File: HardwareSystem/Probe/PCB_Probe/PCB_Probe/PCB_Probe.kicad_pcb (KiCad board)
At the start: 2 copper layers, 37.3 x 162.6 mm, 24 parts, among them J1 Conn_01x15, J2 Conn_01x15, U1 TLC555xP, U2 LP2950CZ-3.0/NOPB

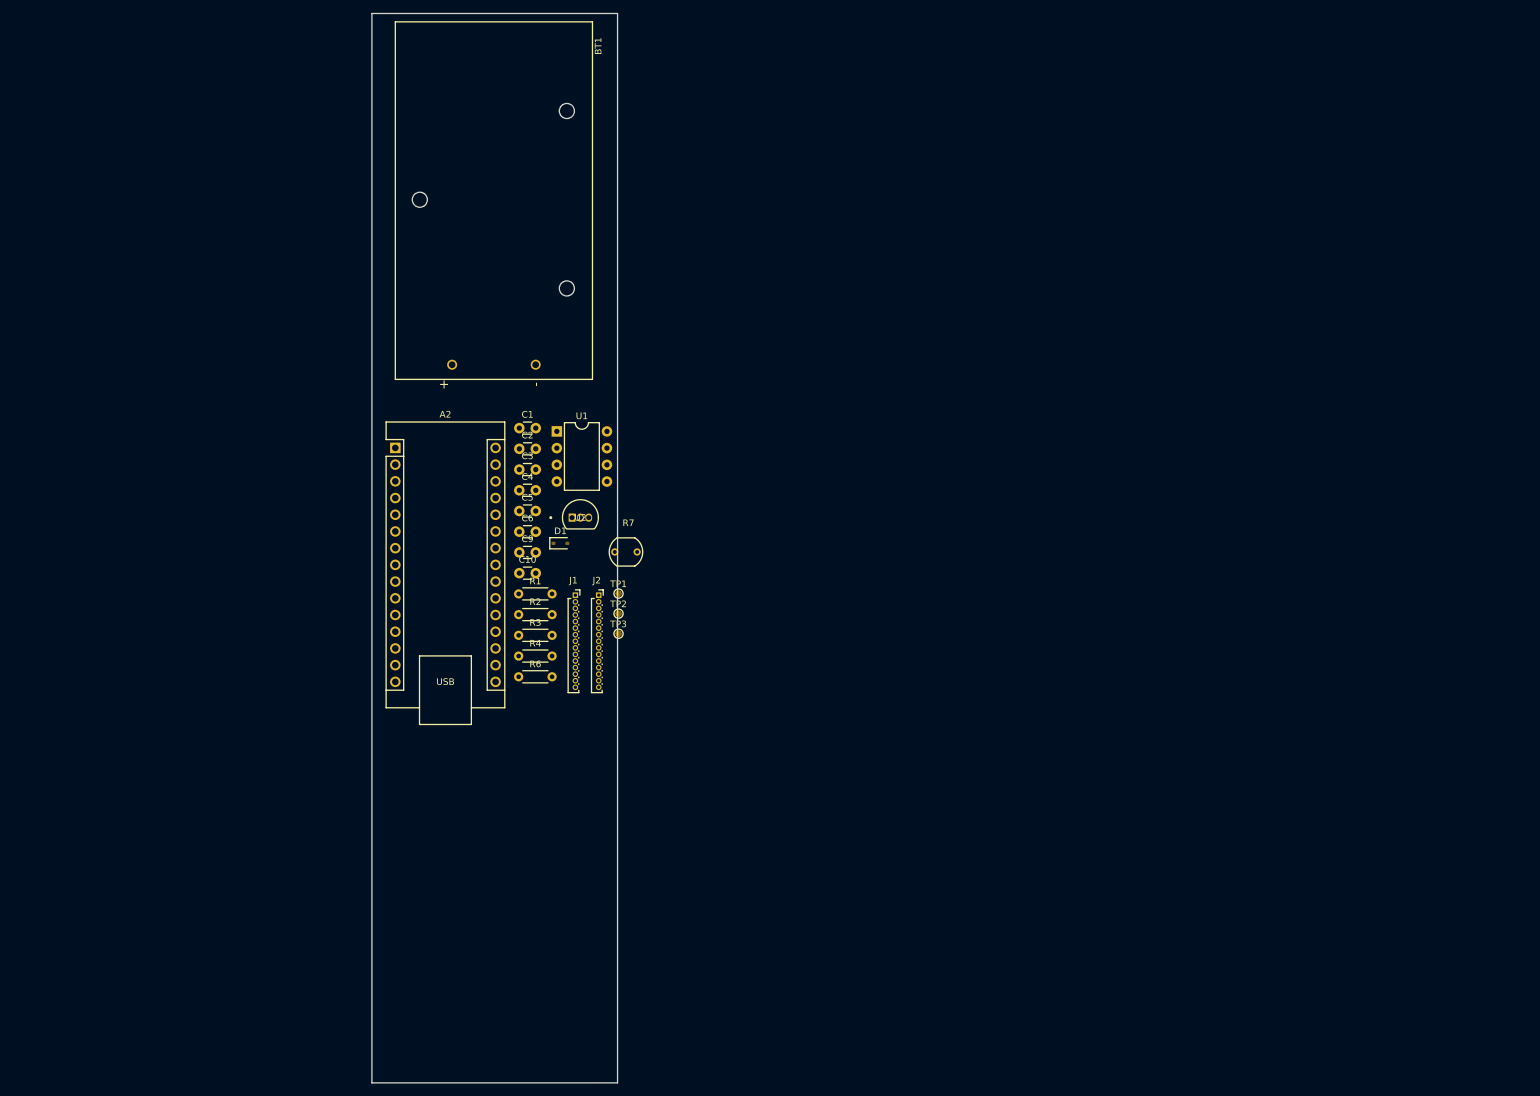
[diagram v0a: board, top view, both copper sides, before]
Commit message: more layout design
Added:
header footprint
pcb margins for probe
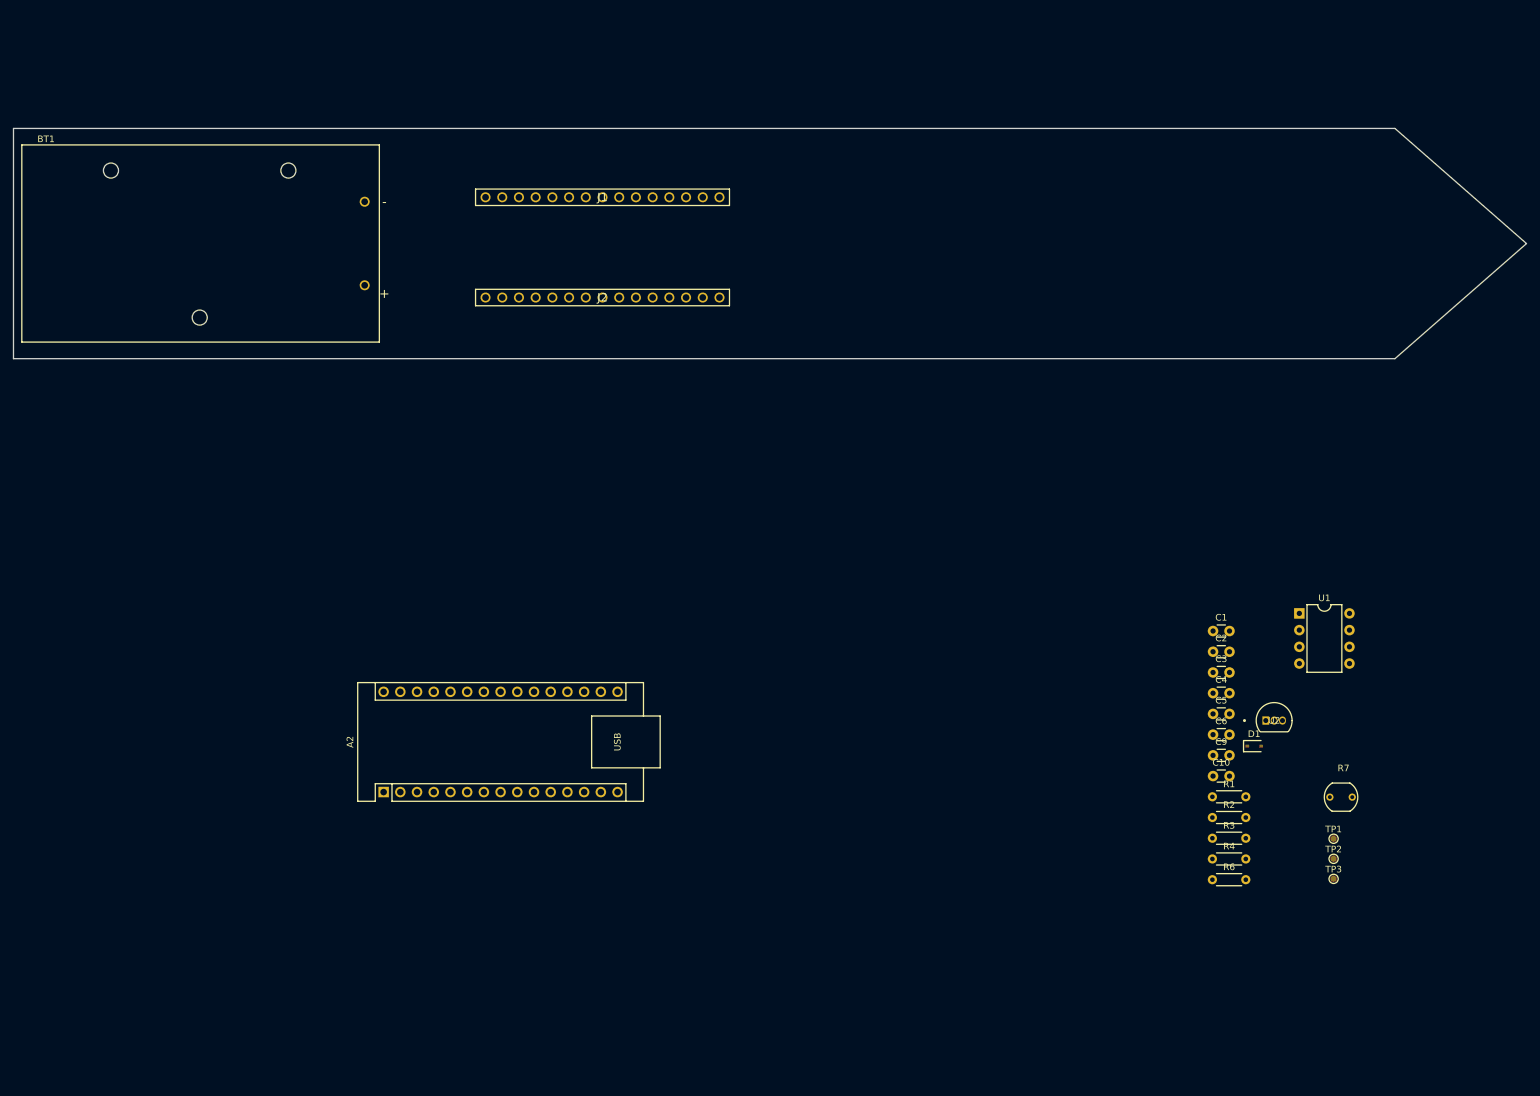
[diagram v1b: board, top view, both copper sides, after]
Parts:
- J1, J2: footprint Connector_PinSocket_1.00mm:PinSocket_1x15_P1.00mm_Vertical -> KiCADv6:PRT16279
- moved U1 116.2 mm to (235.5, 108.7)
- moved R7 114.9 mm to (241.8, 136.7)
- moved TP1 114.9 mm to (240.7, 143.0)
- moved TP2 114.9 mm to (240.7, 146.0)
- moved TP3 114.9 mm to (240.7, 149.1)
- moved D1 109.9 mm to (228.6, 128.9)
- moved R1 109.9 mm to (222.2, 136.6)
- moved R2 109.9 mm to (222.2, 139.8)
- moved R3 109.9 mm to (222.2, 142.9)
- moved R4 109.9 mm to (222.2, 146.1)
- moved R6 109.9 mm to (222.2, 149.2)
- moved U2 109.9 mm to (230.4, 125.0)
- moved C1 109.9 mm to (222.3, 111.4)
- moved C10 109.9 mm to (222.3, 133.4)
- moved C2 109.9 mm to (222.3, 114.5)
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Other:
- board size 37.3 x 162.6 mm -> 230 x 35 mm

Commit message: PCB Probe layout
working on pcb probe layout
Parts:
- removed R7: Photoresistor, KiCADv6:XDCR_161
- added J3: Conn_01x02_Socket, Connector_PinHeader_2.54mm:PinHeader_1x02_P2.54mm_Vertical, F.Cu at (150.1, 39.1)
- added J4: Conn_01x04_Pin, Connector_PinHeader_2.54mm:PinHeader_1x04_P2.54mm_Vertical, F.Cu at (155.4, 66.0)
- added TP4: 3.3V GND Testpoint, TestPoint:TestPoint_Pad_D1.0mm, F.Cu at (71.9, 39.6)
- TP1: value 5V Testpoint -> 9V Testpoint
- moved TP2 203.0 mm to (54.1, 66.0)
- moved TP1 175.1 mm to (86.4, 60.2)
- moved C9 157.8 mm to (86.4, 50.3)
- moved C10 157.3 mm to (86.4, 54.4)
- moved R6 130.6 mm to (153.9, 37.9), turned to -90 degrees
- moved TP3 129.5 mm to (167.3, 42.4)
- moved A2 121.0 mm to (79.8, 16.0), turned to -90 degrees
- moved R4 114.8 mm to (184.7, 37.6), turned to 180 degrees
- moved U2 110.0 mm to (160.4, 40.1)
- moved R3 105.7 mm to (178.8, 46.5)
- moved J1 104.4 mm to (43.9, 60.2), turned to 0 degrees
- moved C6 101.6 mm to (164.5, 43.7), turned to -90 degrees
- moved C5 101.2 mm to (158.9, 45.2)
- moved D1 100.0 mm to (179.6, 41.7), turned to -90 degrees
- moved C4 89.3 mm to (182.2, 41.1)
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
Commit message: Routing and Placement for Probe PCB
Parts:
- removed A2: Arduino_Nano_v3.x, Module:Arduino_Nano
- added H1: MountingHole, MountingHole:MountingHole_3.2mm_M3, F.Cu at (45.0, 66.5)
- added H2: MountingHole, MountingHole:MountingHole_3.2mm_M3, F.Cu at (45.0, 38.5)
- added H3: MountingHole, MountingHole:MountingHole_3.2mm_M3, F.Cu at (87.0, 66.5)
- added H4: MountingHole, MountingHole:MountingHole_3.2mm_M3, F.Cu at (87.6, 38.5)
- added H5: MountingHole, MountingHole:MountingHole_3.2mm_M3, F.Cu at (167.0, 52.5)
- added TP5: Mouisture Testpoint, TestPoint:TestPoint_Pad_D1.0mm, F.Cu at (189.5, 52.5)
- added TP6: Light Testpoint, TestPoint:TestPoint_Pad_D1.0mm, F.Cu at (150.1, 45.0)
- C1, C10, C2, C3, C4, C5, C6, C9: footprint Capacitor_THT:C_Disc_D3.0mm_W1.6mm_P2.50mm -> Capacitor_THT:C_Disc_D4.7mm_W2.5mm_P5.00mm
- D1: value 1N4148WS -> 1N4148; footprint Diode_SMD:D_SOD-323 -> Diode_THT:D_DO-35_SOD27_P7.62mm_Horizontal
- R1, R2, R3, R4, R6: footprint Resistor_THT:R_Axial_DIN0204_L3.6mm_D1.6mm_P5.08mm_Horizontal -> Resistor_THT:R_Axial_DIN0207_L6.3mm_D2.5mm_P10.16mm_Horizontal
- moved R1 28.8 mm to (174.2, 38.6), turned to 180 degrees
- moved R4 27.2 mm to (184.9, 64.8)
- moved C2 23.5 mm to (186.1, 41.9), turned to 180 degrees
- moved C3 22.9 mm to (178.3, 42.4)
- moved R2 21.8 mm to (174.2, 42.2), turned to 180 degrees
- moved C4 21.6 mm to (174.8, 61.5)
- moved D1 20.0 mm to (182.4, 61.5), turned to 0 degrees
- moved C1 17.6 mm to (172.0, 50.0), turned to 90 degrees
- moved R6 11.4 mm to (158.0, 48.5), turned to 180 degrees
- moved R3 10.5 mm to (176.0, 56.6)
- moved TP4 9.68 mm to (81.5, 40.4)
- moved U1 6.81 mm to (177.0, 52.6), turned to 90 degrees
- moved C5 5.91 mm to (153.0, 45.0)
- moved TP3 4.96 mm to (164.1, 46.2)
- moved C6 3.47 mm to (161.0, 44.2)
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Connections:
- BT1 pad -: Pobe -> GND
- C1 pad 1: Pobe -> GND
- C10 pad 2: Pobe -> GND
- C2 pad 2: Pobe -> GND
- C3 pad 1: Pobe -> GND
- C4 pad 2: Pobe -> GND
- C5 pad 1: A_Light -> +3.3V
- C5 pad 2: Pobe -> GND
- C6 pad 2: Pobe -> GND
- C9 pad 2: Pobe -> GND
- J1 pad 2: A_Light -> +3.3V
- J2 pad 12: Pobe -> GND
- J3 pad 1: A_Light -> +3.3V
- J3 pad 2: Net-(J3-Pin_2) -> A_Light
- J4 pad 1: A_Light -> +3.3V
- J4 pad 2: Pobe -> GND
- R4 pad 1: Pobe -> GND
- R6 pad 1: Pobe -> GND
- R6 pad 2: Net-(J3-Pin_2) -> A_Light
- TP2 pad 1: A_Light -> +3.3V
- TP4 pad 1: Pobe -> GND
- U1 pad 1: Pobe -> GND
- U2 pad 1: A_Light -> +3.3V
- U2 pad 2: Pobe -> GND
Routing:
- net GND: track 0.00 -> 189.2 mm
- net +3.3V: track 0.00 -> 156.8 mm
- net A_Moisture: track 0.00 -> 140.5 mm
- net A_Light: track 0.00 -> 107.1 mm, vias 0 -> 1
- net SDA: track 0.00 -> 106.5 mm
- net SCL: track 0.00 -> 100.5 mm, vias 0 -> 1
- net Pobe: track 0.00 -> 88.4 mm
- net +3V0: track 0.00 -> 40.2 mm
- net +9V: track 0.00 -> 29.4 mm
- net Net-(U1-THR): track 0.00 -> 25.0 mm
- net Net-(U1-DIS): track 0.00 -> 23.8 mm
- net Net-(U1-Q): track 0.00 -> 7.79 mm
- net Net-(U1-CV): track 0.00 -> 3.65 mm
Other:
- board size 230 x 35 mm -> 240 x 35 mm
- board text added: "APWS"
- board text added: "APWS-SP10 Jaime Sanchez, Evan LeBel, Ian Skillman, Rodrigo Romero, Alexis Torres, Kiet Le, Javier Padilla, and Jesus Hernandez"

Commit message: updated Probe schematic look
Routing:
- net GND: track 189.2 -> 223.3 mm, vias 0 -> 4
- added copper zone on F.Cu, net GND
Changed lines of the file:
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@@
   (gr_rect (start 40.51 43.558) (end 83.442 61.598)
     (stroke (width 0.15) (type default)) (fill none) (layer "F.SilkS"))
+  (gr_line (start 192.996057 35.166594) (end 193 69.85)
+    (stroke (width 0.15) (type default)) (layer "F.SilkS"))
   (gr_line (start 280 52.5) (end 260 35)
     (stroke (width 0.1) (type default)) (layer "Edge.Cuts"))
@@
   (segment (start 89.949 54.864) (end 89.876 54.864) (width 0.25) (layer "F.Cu") (net 35))
   (segment (start 71.882 44.958) (end 76.454 40.386) (width 0.25) (layer "F.Cu") (net 35))
+  (via (at 192.278 42.926) (size 0.8) (drill 0.4) (layers "F.Cu" "B.Cu") (net 35))
+  (via (at 192.278 41.91) (size 0.8) (drill 0.4) (layers "F.Cu" "B.Cu") (net 35))
+  (via (at 192.278 62.738) (size 0.8) (drill 0.4) (layers "F.Cu" "B.Cu") (free) (net 35))
+  (via (at 192.278 61.722) (size 0.8) (drill 0.4) (layers "F.Cu" "B.Cu") (net 35))
   (segment (start 76.091 49.167) (end 88.751 49.167) (width 0.25) (layer "B.Cu") (net 35))
   (segment (start 177.17663 42.378) (end 171.958 47.59663) (width 0.25) (layer "B.Cu") (net 35))
@@
   (segment (start 179.792 55.312) (end 177.048 52.568) (width 0.25) (layer "B.Cu") (net 35))
   (segment (start 170.728 48.768) (end 161.504 48.768) (width 0.25) (layer "B.Cu") (net 35))
+  (segment (start 191.153 40.785) (end 190.754 40.785) (width 0.25) (layer "B.Cu") (net 35))
   (segment (start 171.958 47.59663) (end 171.958 49.998) (width 0.25) (layer "B.Cu") (net 35))
   (segment (start 161.036 48.006) (end 157.988 44.958) (width 0.25) (layer "B.Cu") (net 35))
@@
   (segment (start 89.876 54.791) (end 89.876 54.356) (width 0.25) (layer "B.Cu") (net 35))
   (segment (start 71.882 44.958) (end 76.091 49.167) (width 0.25) (layer "B.Cu") (net 35))
+  (segment (start 190.754 40.785) (end 182.267 40.785) (width 0.25) (layer "B.Cu") (net 35))
+  (segment (start 192.278 42.926) (end 190.137 40.785) (width 0.25) (layer "B.Cu") (net 35))
+  (segment (start 192.278 61.722) (end 192.278 60.706) (width 0.25) (layer "B.Cu") (net 35))
   (segment (start 155.28 58.842) (end 157.988 56.134) (width 0.25) (layer "B.Cu") (net 35))
   (segment (start 155.28 58.842) (end 154.686 58.842) (width 0.25) (layer "B.Cu") (net 35))
+  (segment (start 190.137 40.785) (end 189.992 40.785) (width 0.25) (layer "B.Cu") (net 35))
   (segment (start 89.876 50.292) (end 89.876 54.864) (width 0.25) (layer "B.Cu") (net 35))
+  (segment (start 181.57 59.69) (end 189.992 59.69) (width 0.25) (layer "B.Cu") (net 35))
+  (segment (start 179.792 61.468) (end 181.57 59.69) (width 0.25) (layer "B.Cu") (net 35))
   (segment (start 159.268 63.424) (end 154.686 58.842) (width 0.25) (layer "B.Cu") (net 35))
+  (segment (start 192.278 41.91) (end 191.153 40.785) (width 0.25) (layer "B.Cu") (net 35))
   (segment (start 99.06 58.842) (end 93.927 58.842) (width 0.25) (layer "B.Cu") (net 35))
   (segment (start 171.958 49.998) (end 170.728 48.768) (width 0.25) (layer "B.Cu") (net 35))
+  (segment (start 191.516 61.976) (end 191.516 60.96) (width 0.25) (layer "B.Cu") (net 35))
+  (segment (start 190.246 59.69) (end 189.992 59.69) (width 0.25) (layer "B.Cu") (net 35))
+  (segment (start 191.516 60.96) (end 190.246 59.69) (width 0.25) (layer "B.Cu") (net 35))
   (segment (start 161.036 49.236) (end 161.036 48.006) (width 0.25) (layer "B.Cu") (net 35))
   (segment (start 178.308 42.378) (end 177.17663 42.378) (width 0.25) (layer "B.Cu") (net 35))
+  (segment (start 192.278 60.706) (end 191.262 59.69) (width 0.25) (layer "B.Cu") (net 35))
   (segment (start 158.202 52.07) (end 161.036 49.236) (width 0.25) (layer "B.Cu") (net 35))
   (segment (start 157.988 52.07) (end 158.202 52.07) (width 0.25) (layer "B.Cu") (net 35))
   (segment (start 157.988 56.134) (end 157.988 52.07) (width 0.25) (layer "B.Cu") (net 35))
   (segment (start 179.792 61.468) (end 179.792 55.312) (width 0.25) (layer "B.Cu") (net 35))
+  (segment (start 189.992 59.69) (end 191.262 59.69) (width 0.25) (layer "B.Cu") (net 35))
+  (segment (start 192.278 62.738) (end 191.516 61.976) (width 0.25) (layer "B.Cu") (net 35))
+  (segment (start 182.267 40.785) (end 181.142 41.91) (width 0.25) (layer "B.Cu") (net 35))
   (segment (start 159.268 67.31) (end 159.268 63.424) (width 0.25) (layer "B.Cu") (net 35))
   (segment (start 153.416 44.958) (end 152.988 44.958) (width 0.25) (layer "F.Cu") (net 36))
@@
   (segment (start 51.562 61.468) (end 54.61 61.468) (width 0.25) (layer "F.Cu") (net 36))
   (segment (start 47.244 61.468) (end 51.562 61.468) (width 0.25) (layer "F.Cu") (net 36))
+  (zone (net 35) (net_name "GND") (layer "F.Cu") (hatch edge 0.5)
+    (connect_pads (clearance 0.5))
+    (min_thickness 0.25) (filled_areas_thickness no)
+    (fill yes (thermal_gap 0.5) (thermal_bridge_width 0.5))
+    (polygon
+      (pts
+        (xy 191.516 40.132)
+        (xy 263.398 40.132)
+        (xy 277.622 52.578)
+        (xy 263.652 64.262)
+        (xy 191.51742 64.607202)
+        (xy 191.516 60.96)
+        (xy 193.04 60.96)
+        (xy 263.144 60.96)
+        (xy 274.574 52.578)
+        (xy 263.398 43.434)
+        (xy 191.516 43.434)
+      )
+    )
+  )
   (zone locked (net 0) (net_name "") (layer "Margin") (name "AHT20") (hatch edge 0.5)
     (connect_pads (clearance 0))
